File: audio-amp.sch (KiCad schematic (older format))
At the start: 48 parts, among them J1 AUDIO IN, J2 LEFT, J3 RIGHT, J4 24VDC, U1 TPA313xD2

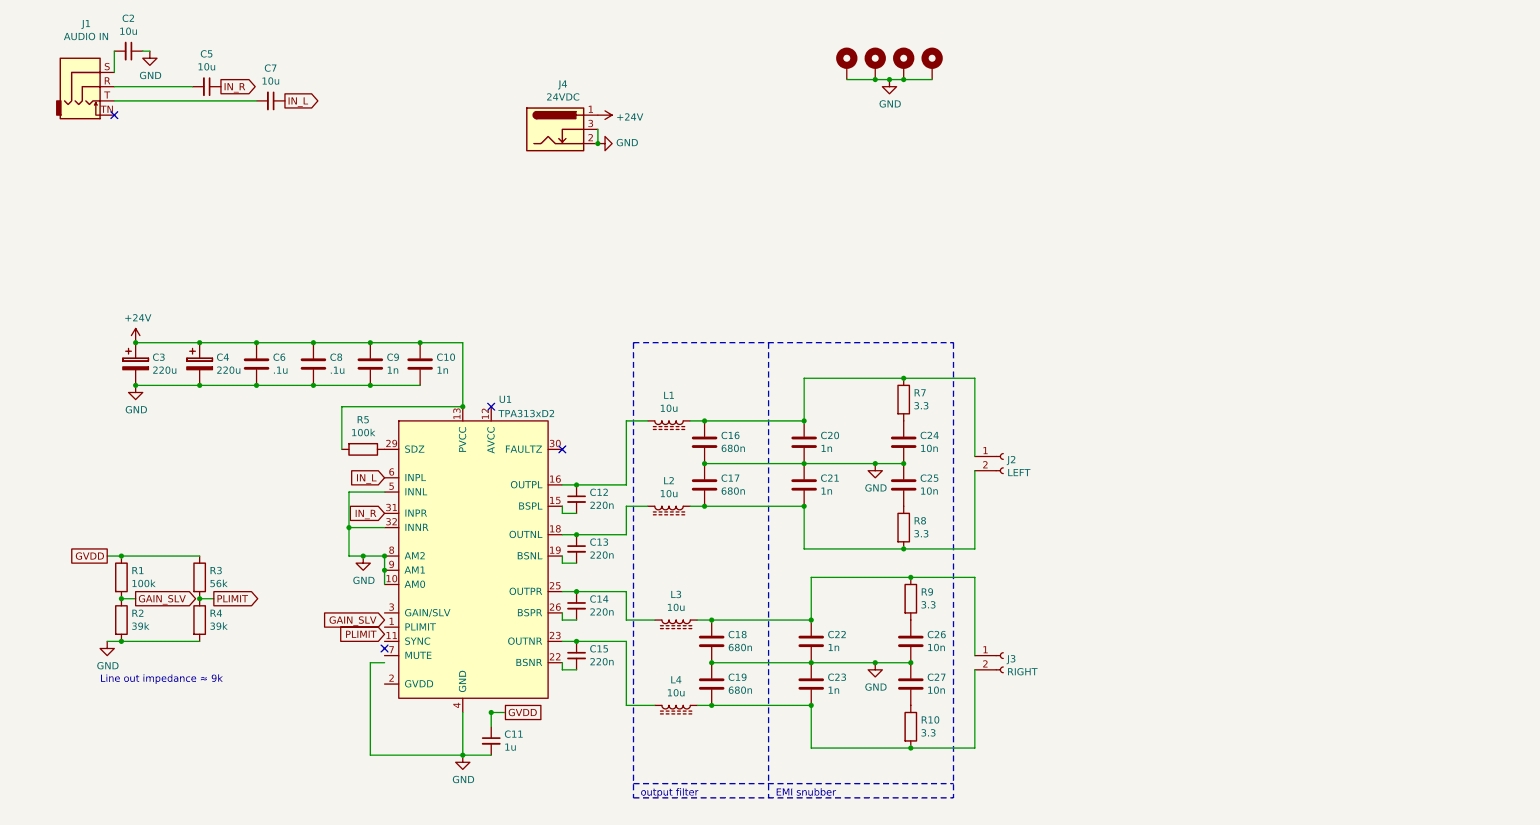
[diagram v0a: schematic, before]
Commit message: Add datasheets
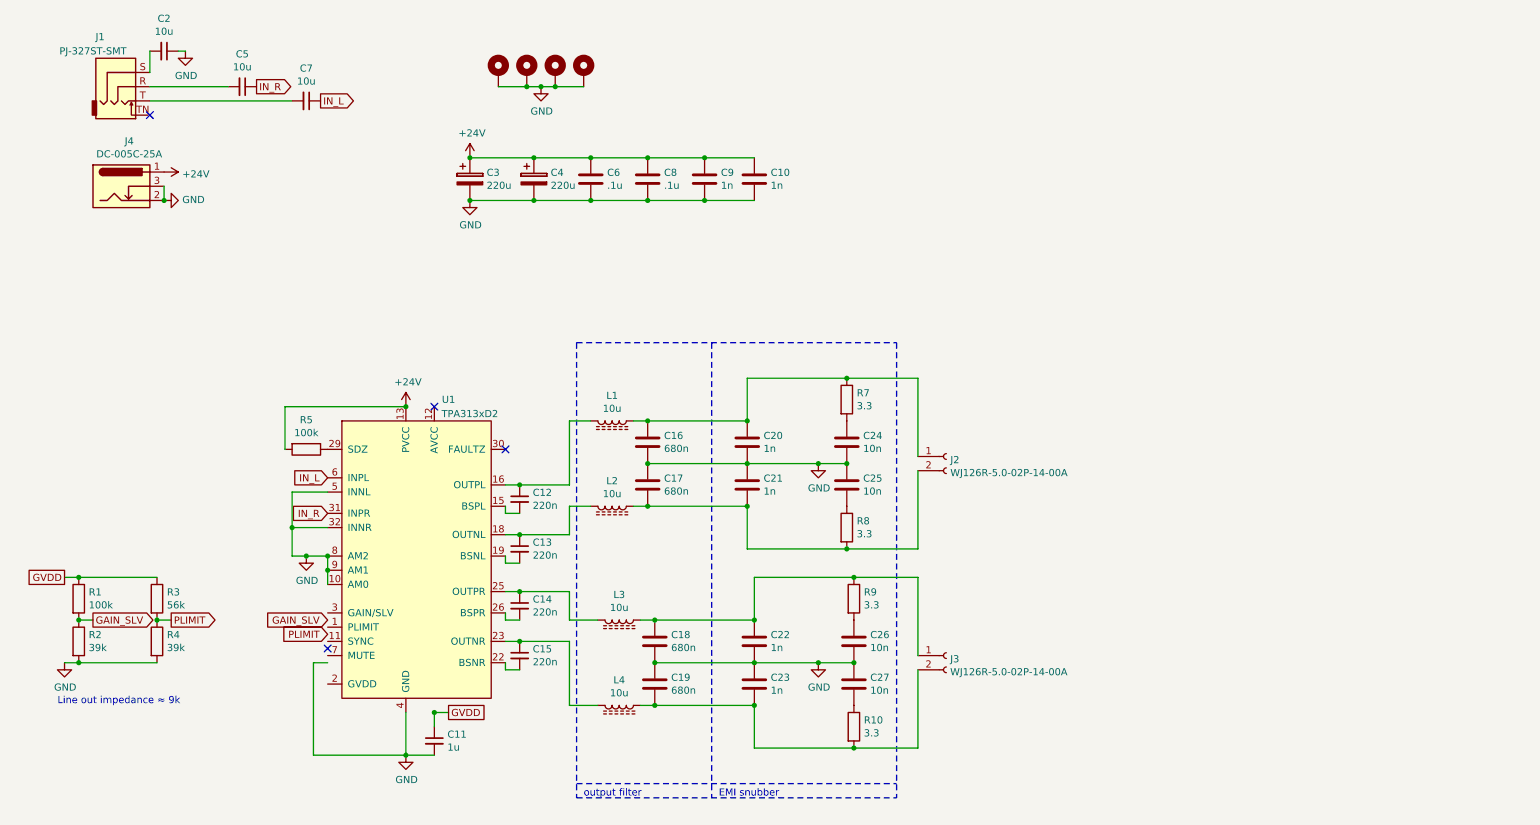
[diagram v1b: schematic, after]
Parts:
- J1: value AUDIO IN -> PJ-327ST-SMT
- J2: value LEFT -> WJ126R-5.0-02P-14-00A
- J3: value RIGHT -> WJ126R-5.0-02P-14-00A
- J4: value 24VDC -> DC-005C-25A
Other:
- moved on the sheet: C10, C11, C12, C13, C14, C15, C16, C17, C18, C19, C2, C20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

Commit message: progress on v2.
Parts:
- removed C20, C21, C22, C23: 1n, Capacitor_SMD:C_0603_1608Metric_Pad1.05x0.95mm_HandSolder, symbol Device:C
- removed C24, C25, C26, C27: 10n, Capacitor_SMD:C_0603_1608Metric_Pad1.05x0.95mm_HandSolder, symbol Device:C
- removed J2, J3: WJ126R-5.0-02P-14-00A, OSTTA020161:OST_OSTTA020161, symbol Connector:Conn_01x02_Female
- removed R10, R7, R8, R9: 3.3, Resistor_SMD:R_0603_1608Metric_Pad1.05x0.95mm_HandSolder, symbol Device:R
- added C3: 10u, Capacitor_SMD:C_0805_2012Metric_Pad1.15x1.40mm_HandSolder, symbol Device:C_Small
- added J3: WJ126-5.0, symbol Connector_Generic:Conn_01x04
- added JP1, JP2: Jumper_2_Open, Jumper:SolderJumper-2_P1.3mm_Open_RoundedPad1.0x1.5mm, symbol Jumper:Jumper_2_Open
- added R6: 39k, Resistor_SMD:R_0603_1608Metric_Pad1.05x0.95mm_HandSolder, symbol Device:R
- added TP1, TP2, TP3, TP4, TP5, TP6, TP7, TP8, TP9: TestPoint, TestPoint:TestPoint_THTPad_D2.0mm_Drill1.0mm, symbol Connector:TestPoint
- C14: renamed from C16; value 680n -> 1u
- C15: renamed from C17; value 680n -> 1u
- C16: renamed from C18; value 680n -> 1u
- C17: renamed from C19; value 680n -> 1u
- renumbered C5 to C1, C15 to C10, C4 to C11, C6 to C12, C8 to C13, C9 to C18, C10 to C19, C7 to C4, C11 to C5, C3 to C6, C12 to C7, C13 to C8, C14 to C9, J4 to J2
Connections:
- net +24V: now also U1.12 (AVCC), R6.1, TP3.1
- net GAIN_SLV: now also U1.3 (GAIN/SLV)
- net GND: now also C2.2, U1.7 (MUTE), C3.2, JP1.2 (B), JP2.2 (B), R6.2, TP4.1; no longer C2.1, U1.32 (INNR), U1.5 (INNL)
- net GVDD: now also U1.2 (GVDD)
- net IN_L: now also JP1.1 (A)
- net PLIMIT: now also U1.1 (PLIMIT)
- net at C1.2, J1.R: now also TP2.1
- net at J1.S: now also TP1.1; no longer C2.2
- net at C4.2, J1.T: now also TP5.1
- net at C14.1, L1.1: now also J3.1 (Pin_1), TP6.1
- net at C15.2, L2.1: now also J3.2 (Pin_2), TP7.1
- net at C16.1, L3.1: now also J3.3 (Pin_3), TP8.1
- net at C17.2, L4.1: now also J3.4 (Pin_4), TP9.1
- new net: C3.1, U1.32 (INNR)
- new net IP_L: C2.1, JP2.1 (A), U1.5 (INNL)
- no-connect marks 4 -> 3
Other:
- note removed: "EMI snubber"
- moved on the sheet: C1, C16, C17, C4, C5, J2, L3, L4

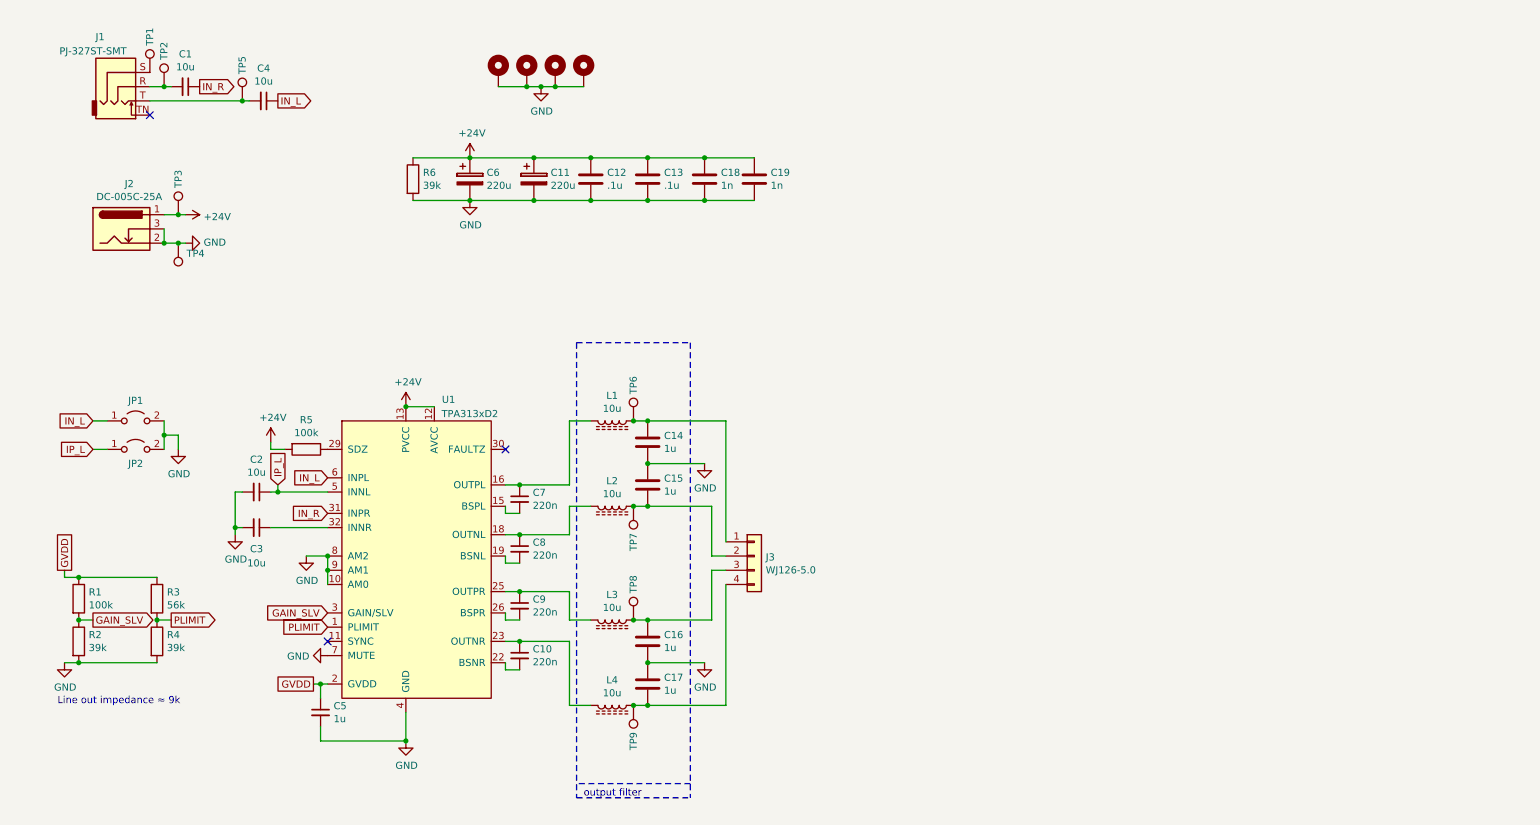
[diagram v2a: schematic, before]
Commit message: Rev 2 done (probably)
This revision has

1. Correct capacitor filtering, with well-matched differential traces
2. The fault pin is no longer floating
3. The fault pin is now tied to the enable pin, allowing for
auto-restarting every 2 seconds.
4. The PVCC pin is now connected to power, instead of being left
disconnected like in the reference design.
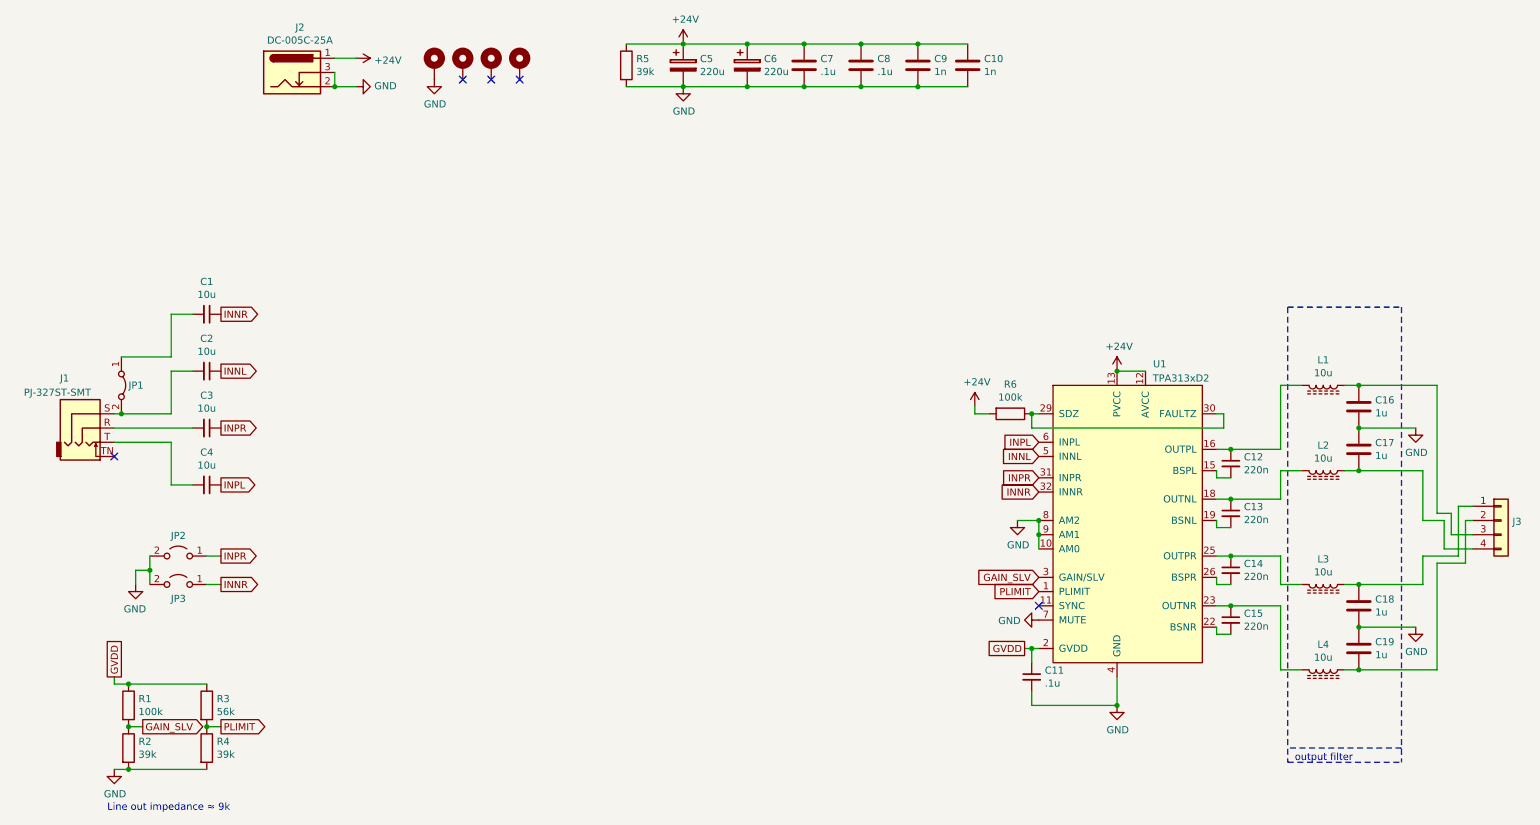
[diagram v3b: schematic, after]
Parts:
- removed C3: 10u, Capacitor_SMD:C_0805_2012Metric_Pad1.15x1.40mm_HandSolder, symbol Device:C_Small
- removed TP1, TP2, TP3, TP4, TP5, TP6, TP7, TP8, TP9: TestPoint, TestPoint:TestPoint_THTPad_D2.0mm_Drill1.0mm, symbol Connector:TestPoint
- added C1: 10u, Capacitor_SMD:C_0805_2012Metric_Pad1.15x1.40mm_HandSolder, symbol Device:C_Small
- added JP1: Jumper_2_Bridged, Jumper:SolderJumper-2_P1.3mm_Open_RoundedPad1.0x1.5mm, symbol Jumper:Jumper_2_Bridged
- C11: renamed from C5; value 1u -> .1u
- J3: footprint (none) -> audio-amp:DG301_G-1x04_P5.0mm_Horizontal
- renumbered C19 to C10, C7 to C12, C8 to C13, C9 to C14, C10 to C15, C14 to C16, C15 to C17, C16 to C18, C17 to C19, C1 to C3, C6 to C5, C11 to C6, C12 to C7, C13 to C8, C18 to C9, H3 to H1, H1 to H2, H2 to H3, JP1 to JP2, JP2 to JP3, R6 to R5, R5 to R6
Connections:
- net GND: no longer C2.2, H2.1, H3.1, H4.1
- net at R6.1, U1.29 (SDZ): now also U1.30 (FAULTZ)
- net INNR: now reaches U1.32 (INNR)
- net INNR: now also JP3.1 (A), C1.1
- net at J1.S: now also C2.2, JP1.2 (B)
- net at C16.1, L1.1: now also J3.3 (Pin_3); no longer J3.1 (Pin_1)
- net at C17.2, L2.1: now also J3.4 (Pin_4); no longer J3.2 (Pin_2)
- net at C18.1, L3.1: now also J3.1 (Pin_1); no longer J3.3 (Pin_3)
- net at C19.2, L4.1: now also J3.2 (Pin_2); no longer J3.4 (Pin_4)
- net IN_L renamed INPL
- net INPL: no longer JP2.1 (A)
- net IN_R renamed INPR
- net INPR: now also JP2.1 (A)
- net IP_L renamed INNL
- net INNL: no longer JP3.1 (A)
- new net: C1.2, JP1.1 (A)
- no-connect marks 3 -> 5
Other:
- moved on the sheet: C10, C11, C12, C13, C14, C15, C16, C17, C18, C19, C3, C4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
